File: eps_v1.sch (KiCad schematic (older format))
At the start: 23 parts, among them J7 PROGRAMMING PORT, J8 H_EPS, J9 DEBUG, SW1 SW_RST, U1 ATMEGA32M1-MU, U10 ADS7952, U18 ADS7952, U8 SN65HVD230, U9 SST25VF016B, Y1 8MHz

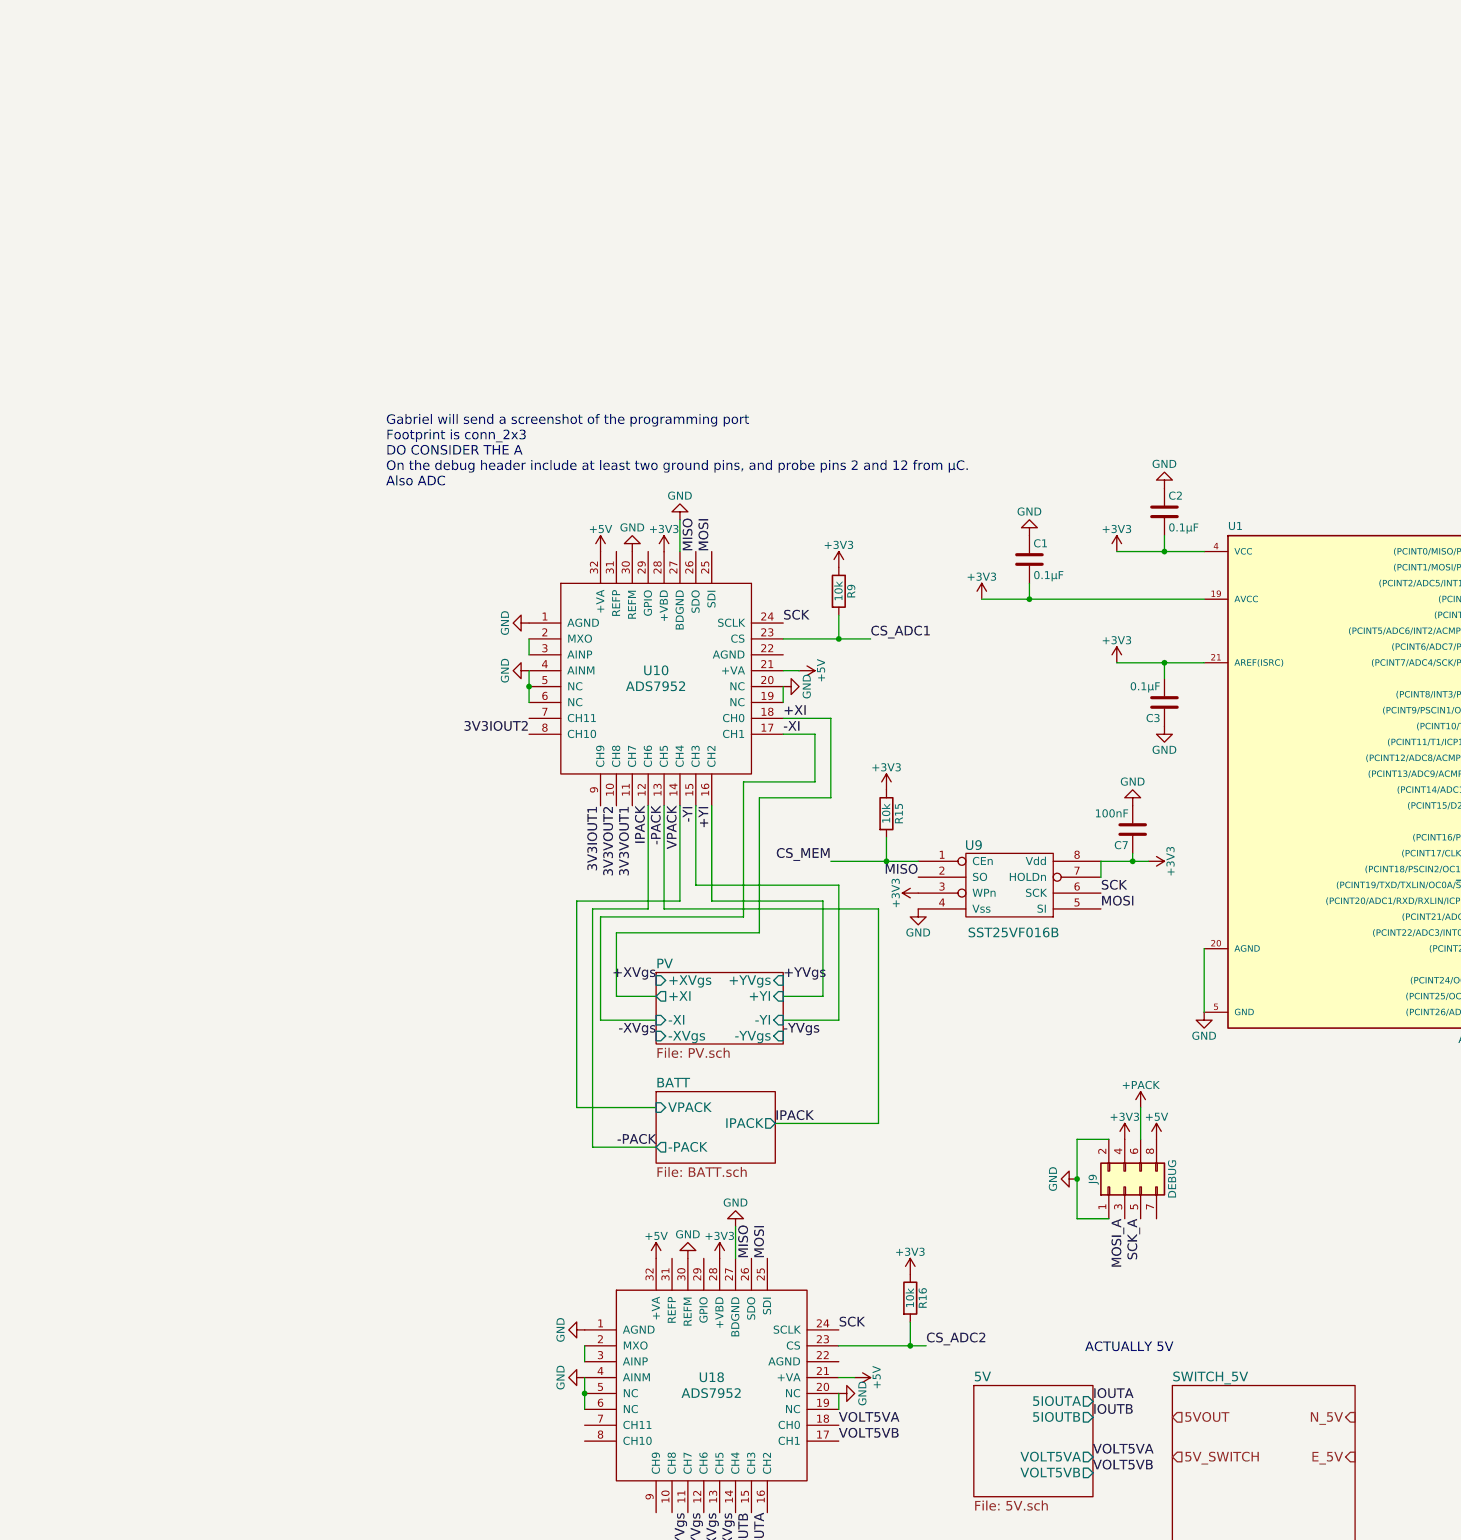
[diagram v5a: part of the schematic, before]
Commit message: Added REF5025 for 2.5V reference for ADCs
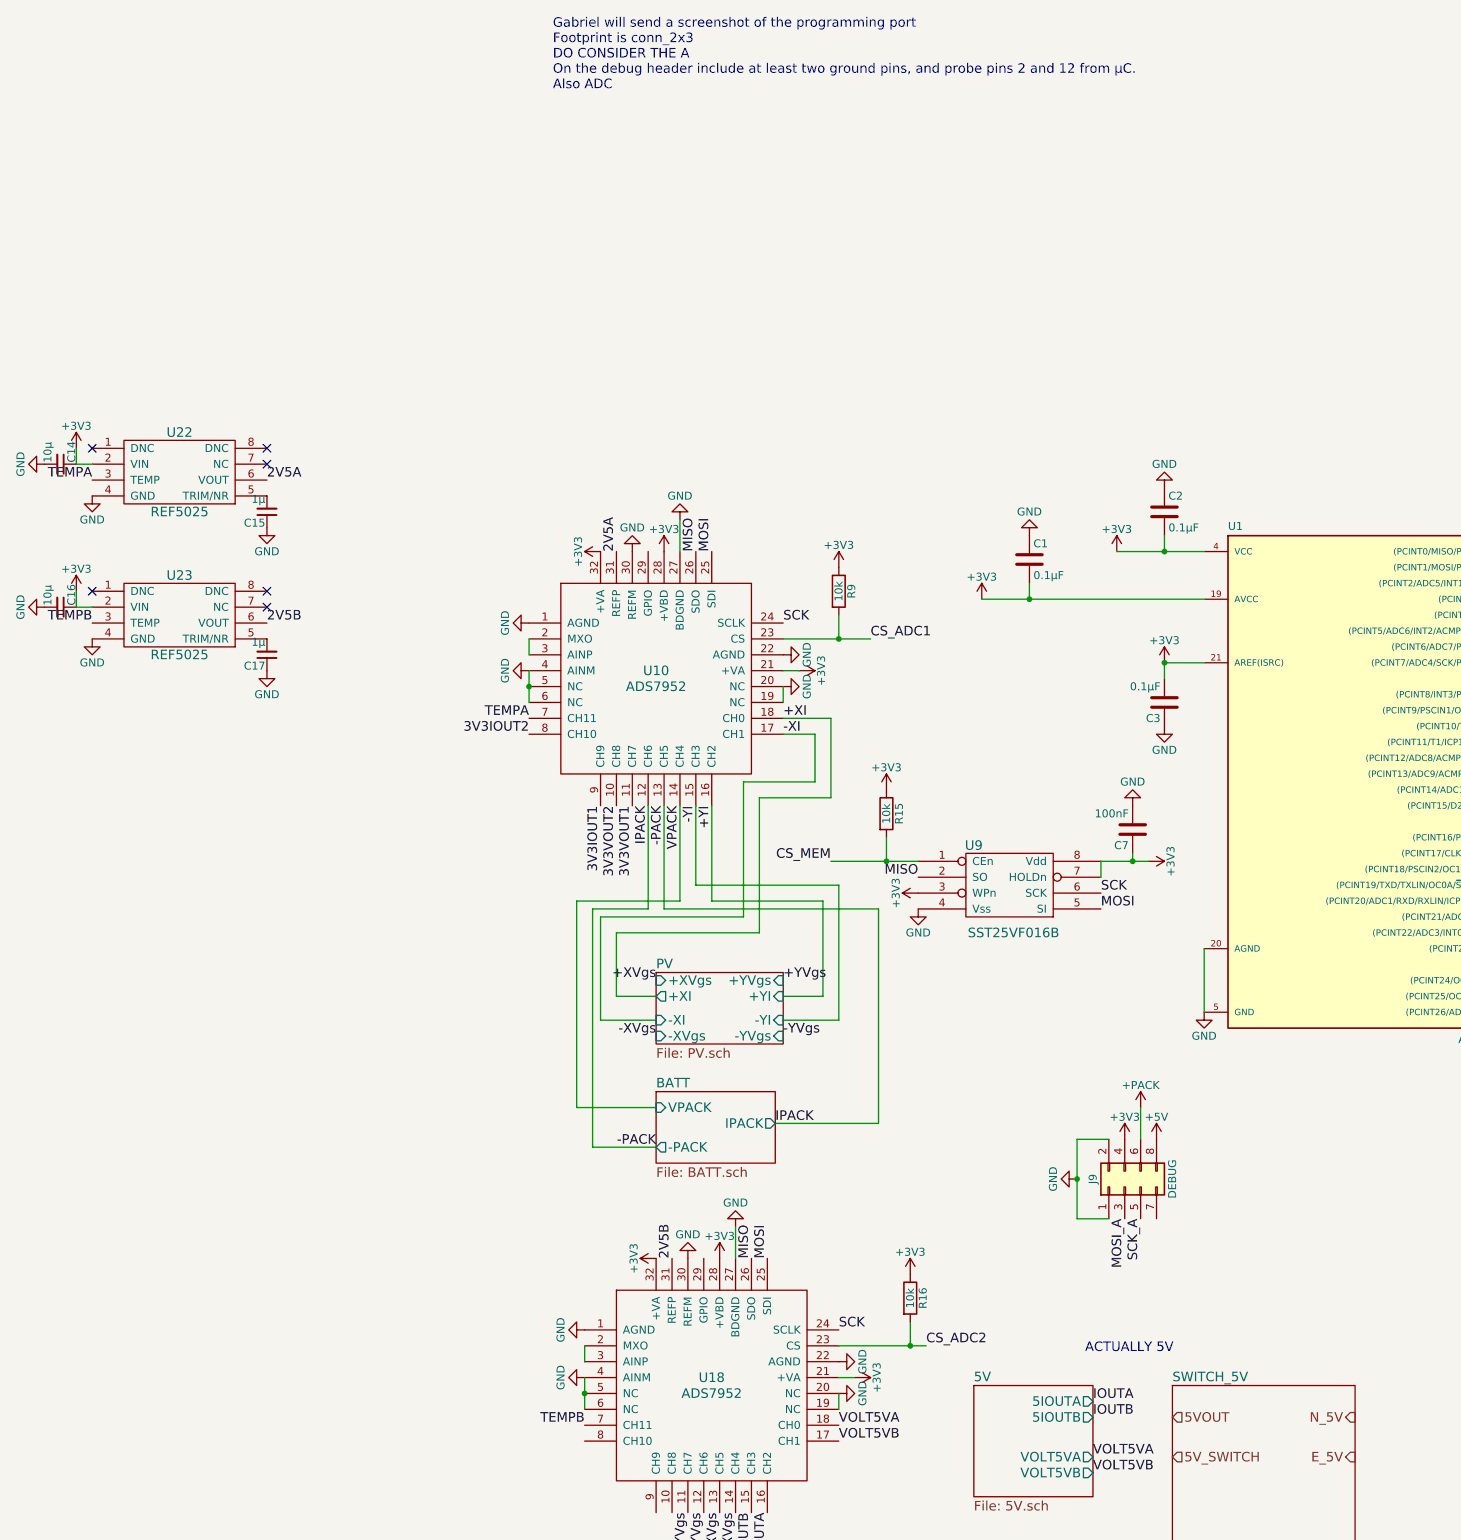
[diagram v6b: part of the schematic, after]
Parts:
- added C14, C16: 10µ, Capacitors_SMD:C_0603_HandSoldering, symbol C_Small
- added C15, C17: 1µ, Capacitors_SMD:C_0603_HandSoldering, symbol C_Small
- added U22, U23: REF5025, symbol REF5025
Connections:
- net +3V3: now also U10.21 (+VA), U10.32 (+VA), U18.21 (+VA), U18.32 (+VA), C14.1, C16.1, U22.2 (VIN), U23.2 (VIN)
- net +5V: no longer U10.21 (+VA), U10.32 (+VA), U18.21 (+VA), U18.32 (+VA)
- net GND: now also U10.22 (AGND), U18.22 (AGND), C14.2, C15.1, C16.2, C17.1, U22.4 (GND), U23.4 (GND)
- net 2V5A: now reaches U10.31 (REFP)
- net 2V5A: now also U22.6 (VOUT)
- net TEMPA: now reaches U10.7 (CH11)
- net TEMPA: now also U22.3 (TEMP)
- net 2V5B: now reaches U18.31 (REFP)
- net 2V5B: now also U23.6 (VOUT)
- net TEMPB: now reaches U18.7 (CH11)
- net TEMPB: now also U23.3 (TEMP)
- new net: C15.2, U22.5 (TRIM/NR)
- new net: C17.2, U23.5 (TRIM/NR)
- no-connect marks 4 -> 10

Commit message: Added/Removed Misc Datasheets
Added TPS630250 and removed TPS 630242 design.
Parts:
- U22, U23: footprint (none) -> Housings_SOIC:SOIC-8_3.9x4.9mm_Pitch1.27mm
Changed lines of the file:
@@
 F 0 "U22" H -1450 1050 60  0000 C CNN
 F 1 "REF5025" H -1450 550 60  0000 C CNN
-F 2 "" H -1450 800 60  0001 C CNN
+F 2 "Housings_SOIC:SOIC-8_3.9x4.9mm_Pitch1.27mm" H -1450 800 60  0001 C CNN
 F 3 "" H -1450 800 60  0001 C CNN
 	1    -1450 800
@@
 F 0 "U23" H -1450 1950 60  0000 C CNN
 F 1 "REF5025" H -1450 1450 60  0000 C CNN
-F 2 "" H -1450 1700 60  0001 C CNN
+F 2 "Housings_SOIC:SOIC-8_3.9x4.9mm_Pitch1.27mm" H -1450 1700 60  0001 C CNN
 F 3 "" H -1450 1700 60  0001 C CNN
 	1    -1450 1700
